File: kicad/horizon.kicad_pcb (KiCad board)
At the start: 2 copper layers, 266 x 76 mm, 117 parts, among them SW1 SW_Push, SW10 SW_Push, SW11 SW_Push, SW12 SW_Push, SW13 SW_Push, SW14 SW_Push, SW15 SW_Push, SW16 SW_Push, SW17 SW_Push, SW18 SW_Push, SW19 SW_Push, SW2 SW_Push, SW20 SW_Push, SW21 SW_Push, SW22 SW_Push, SW23 SW_Push, SW24 SW_Push, SW25 SW_Push, SW26 SW_Push, SW27 SW_Push, SW28 SW_Push, SW29 SW_Push, SW3 SW_Push, SW30 SW_Push, SW31 SW_Push, SW32 SW_Push, SW33 SW_Push, SW34 SW_Push, SW35 SW_Push, SW36 SW_Push, SW37 SW_Push, SW38 SW_Push, SW39 SW_Push, SW4 SW_Push, SW40 SW_Push, SW41 SW_Push, SW42 SW_Push, SW43 SW_Push, SW44 SW_Push, SW45 SW_Push, SW46 SW_Push, SW47 SW_Push, SW48 SW_Push, SW49 SW_Push, SW5 SW_Push, SW50 SW_Push, SW51 SW_Push, SW52 SW_Push, SW6 SW_Push, SW7 SW_Push, SW8 SW_Push, SW9 SW_Push, U1 PRO-MICRO

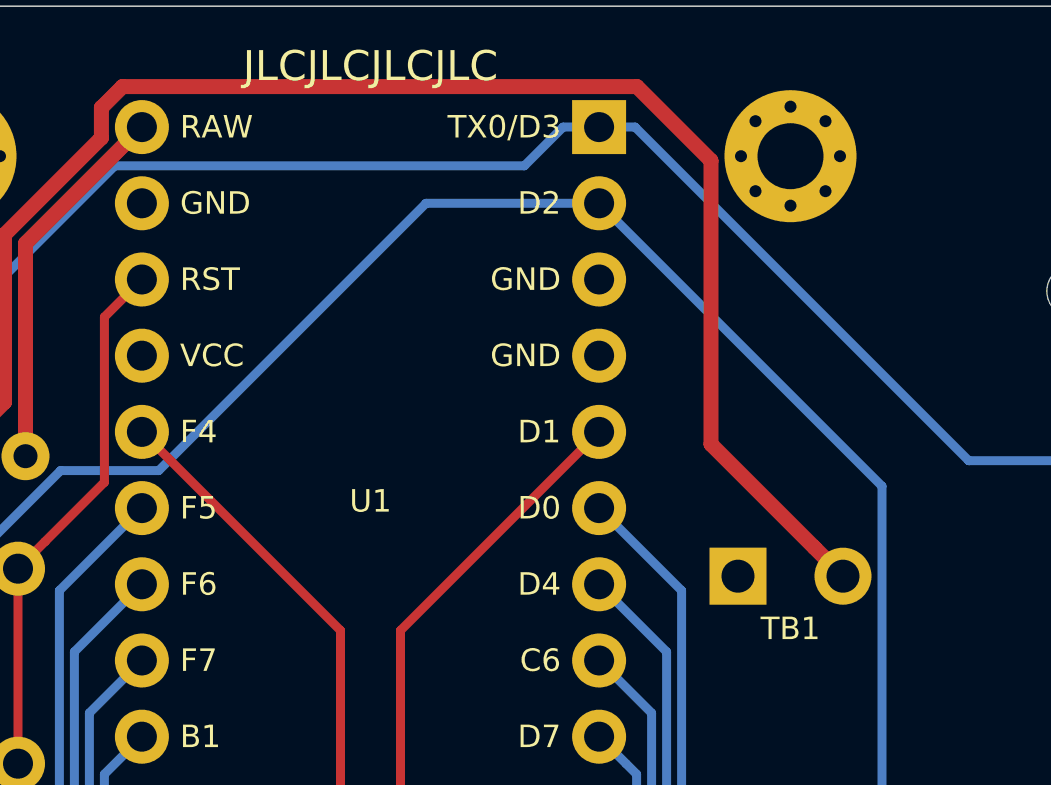
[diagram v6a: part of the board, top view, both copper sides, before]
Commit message: Mark bottom plate cutout on footprint adhesive layer. Begin writing bottom plate generation script
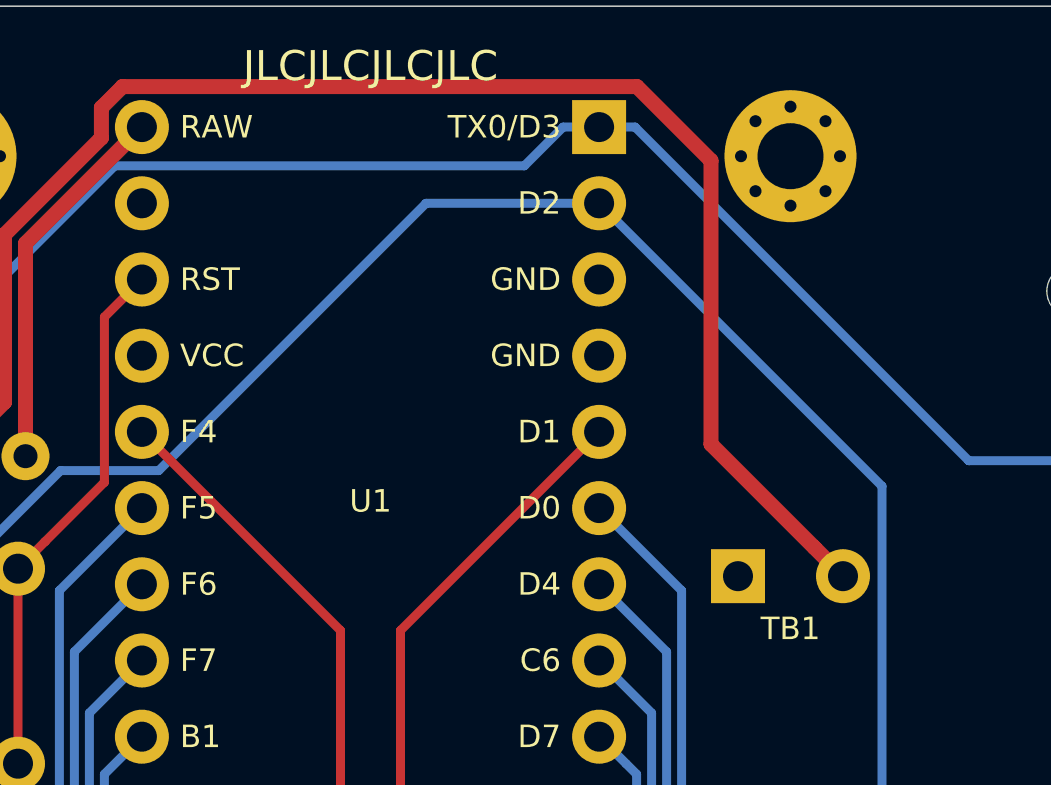
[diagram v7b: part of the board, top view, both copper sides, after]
